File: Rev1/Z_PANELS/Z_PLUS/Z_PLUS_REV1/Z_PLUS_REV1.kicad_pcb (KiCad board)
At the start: 4 copper layers, 98 x 98 mm, 55 parts, among them IC1 LTC4316IDD#PBF, IC2 SM141K04TFV, IC3 SM141K04TFV, IC4 SM141K04TFV, IC5 SM141K04TFV, J1 F3311A7H121014E200, Q1 BSS138, Q2 BSS138, Q3 MBT2222ADW1T1, Q4 BSS138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

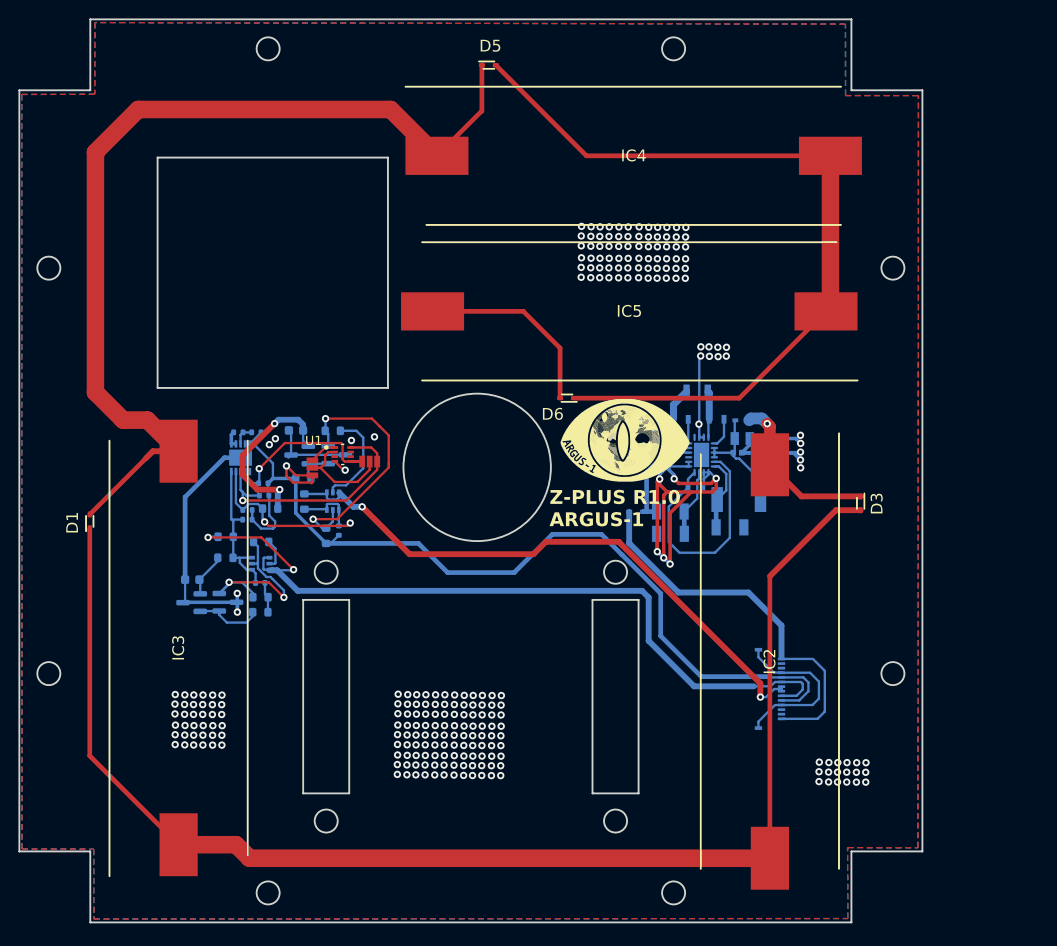
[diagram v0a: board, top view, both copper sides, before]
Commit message: finished Z minus board design
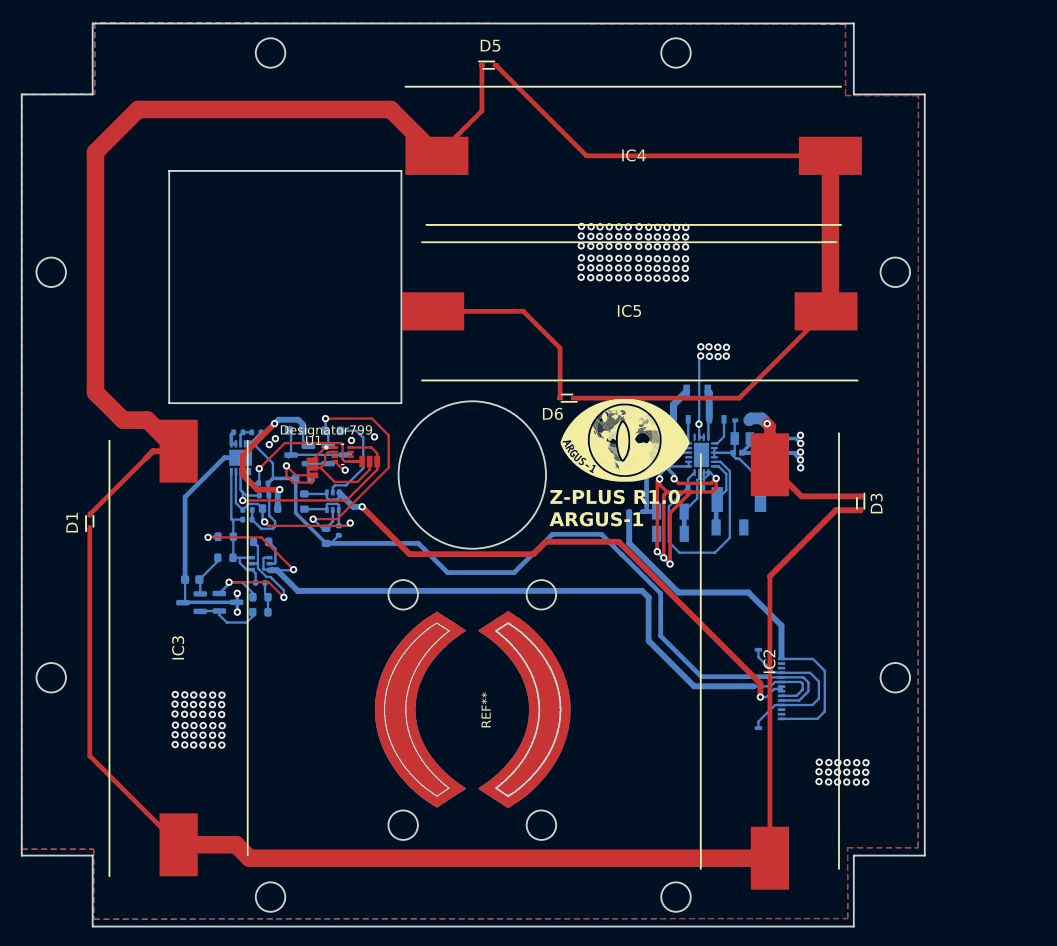
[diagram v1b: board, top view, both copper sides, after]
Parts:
- added REF**: Radio_antenna, Audio_Module:Radio_antenna, F.Cu at (171.7, 108.3)
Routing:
- net GND: vias 262 -> 154
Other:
- outline, holes or cut-outs redrawn

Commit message: fixed bug in Z minus
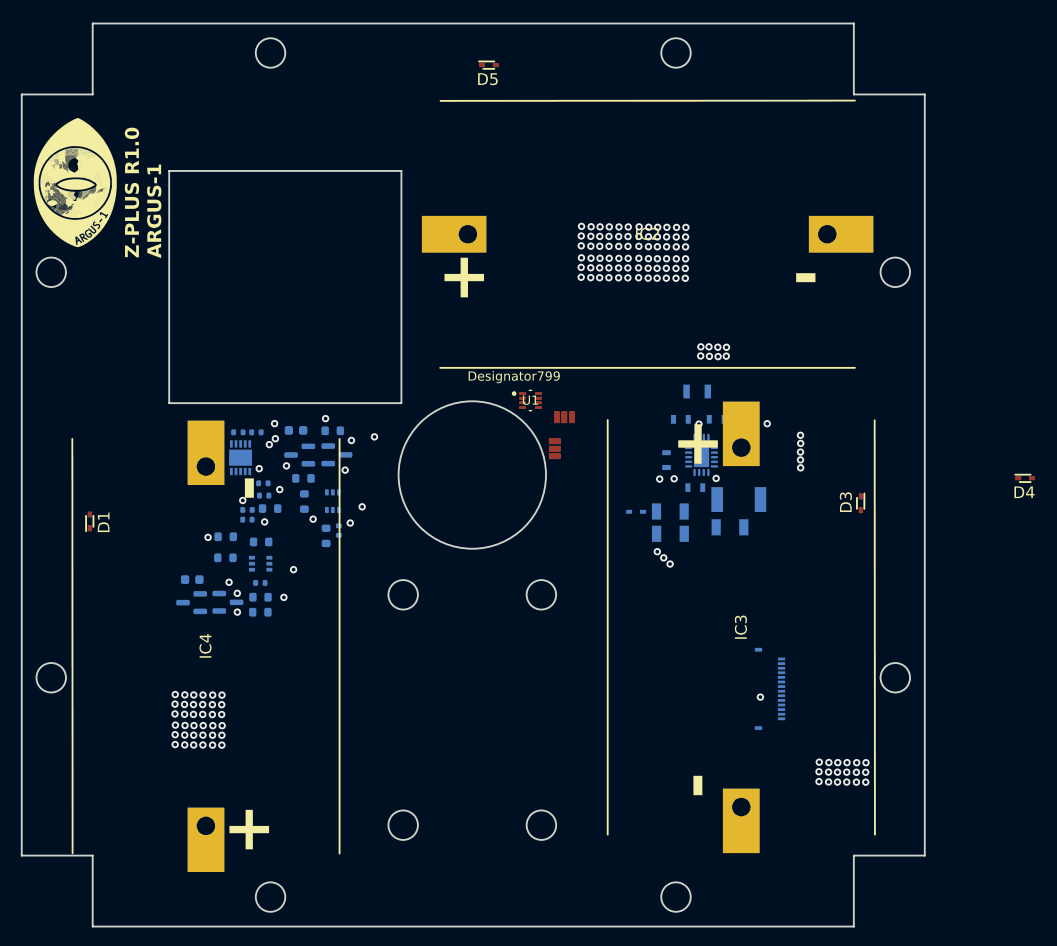
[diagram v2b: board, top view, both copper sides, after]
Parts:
- removed D6, D7: RB521S30T1G, AA_AUTO_LOADER:SODFL1608X70N
- removed IC5: SM141K04TFV, AA_AUTO_LOADER:SODFL490150X120N
- removed REF**: Radio_antenna, Audio_Module:Radio_antenna
- added D4: RB521S30T1G, AA_AUTO_LOADER:SODFL1608X70N, F.Cu at (229.7, 83.1)
- C3: value CL21A476MQYNNNE -> 47uF
- C4: value CL05A105KQ5NNNC -> 1uF
- C5, C8: value CL10A475KQ8NNNC -> 4.7uF
- IC2, IC3, IC4: value SM141K04TFV -> SM141K08TFV; footprint AA_AUTO_LOADER:SODFL490150X120N -> AA_AUTO_LOADER:SODFL520290X120N
- moved IC4 70.6 mm to (140.8, 101.3), turned to 90 degrees
- moved . 65.6 mm to (126.5, 51.2), turned to 90 degrees
- moved IC3 61.1 mm to (198.9, 99.3), turned to -90 degrees
- moved IC2 48.2 mm to (188.7, 56.6), turned to 0 degrees
- moved JP2 26.4 mm to (178.6, 79.9)
- moved JP1 21.7 mm to (179.7, 76.5)
- moved U1 21.2 mm to (176.0, 74.7)
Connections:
- C3 pad 1: GND -> Net-(U2-PVIN)
- C3 pad 2: Net-(U2-PVIN) -> GND
- C4 pad 1: GND -> Net-(U2-PVIN)
- C4 pad 2: Net-(U2-PVIN) -> GND
- C5 pad 1: GND -> Net-(U2-VCC)
- C5 pad 2: Net-(U2-VCC) -> GND
- C8 pad 1: GND -> Net-(U2-VOUT)
- C8 pad 2: Net-(U2-VOUT) -> GND
- D1 pad 1: Net-(IC2-NEG) -> /SOLAR_PANEL_ELECTRONICS/7023_vout
- D1 pad 2: Net-(IC3-NEG) -> Net-(IC2-NEG)
- D2 pad 1: VSOLAR -> Net-(IC2-NEG)
- D2 pad 2: Net-(U2-VOUT) -> Net-(IC3-NEG)
- D3 pad 1: /SOLAR_PANEL_ELECTRONICS/7023_vout -> Net-(U2-PVIN)
- D3 pad 2: Net-(IC2-NEG) -> /SOLAR_PANEL_ELECTRONICS/7023_vout
- D5 pad 1: Net-(IC3-NEG) -> VSOLAR
- D5 pad 2: Net-(IC4-NEG) -> Net-(U2-VOUT)
- IC4 pad 2: Net-(IC4-NEG) -> GND
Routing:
- net GND: track 169.3 -> 0.00 mm
- net Net-(IC2-NEG): track 146.5 -> 0.00 mm
- net Net-(IC3-NEG): track 103.1 -> 0.00 mm, vias 0 -> 1
- net +3.3V: track 102.1 -> 0.00 mm
- net Net-(IC4-NEG): track 88.1 -> 0.00 mm
- net SCL1_b4iso: track 86.0 -> 0.00 mm
- net SDA1_b4iso: track 65.2 -> 0.00 mm
- net VSOLAR: track 41.8 -> 0.00 mm
- net Net-(Q4-S): track 28.9 -> 0.00 mm, vias 2 -> 1
- net SDA_SUN: track 26.3 -> 0.00 mm
- net SDA_4001: track 26.3 -> 0.00 mm
- net Net-(U2-VCC): track 25.8 -> 0.00 mm
- net Net-(Q1-S): track 21.7 -> 0.00 mm
- net Net-(Q5-G): track 19.9 -> 0.00 mm
- net SCL_4001: track 19.4 -> 0.00 mm
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- removed copper zone on B.Cu, net GND
- removed copper zone on F.Cu, net GND

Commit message: fixed bugs and finished Z plus
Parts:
- added FL1: DXW21HN5011BL, AA_AUTO_LOADER:DXW21HN5011BL, B.Cu at (169.9, 95.7)
- added J2: 73412-0114, AA_AUTO_LOADER:73412-0110, B.Cu at (152.3, 93.2)
- added J3: Tape_Measure_Antenna, Audio_Module:Radio_antenna, F.Cu at (171.7, 108.3)
- C3: footprint AA_AUTO_LOADER:CAPC2012X135N -> Capacitor_SMD:C_0805_2012Metric
- C4: footprint AA_AUTO_LOADER:CAPC1005X55N -> Capacitor_SMD:C_0805_2012Metric
- C5, C8: footprint AA_AUTO_LOADER:CAPC1608X90N -> Capacitor_SMD:C_0805_2012Metric
- D2: moved to F.Cu
- D3, D5: moved to B.Cu
- R1, R10, R17, R2, R5, R6: footprint Resistor_SMD:R_0402_1005Metric -> Resistor_SMD:R_0805_2012Metric
- R11, R14, R15, R16, R18, R7, R8, R9: footprint Resistor_SMD:R_0603_1608Metric -> Resistor_SMD:R_0805_2012Metric
- R3, R4: footprint Resistor_SMD:R_0402_1005Metric -> Resistor_SMD:R_0805_2012Metric; moved to F.Cu
- moved D4 110.0 mm to (124.8, 116.5), turned to 90 degrees
- moved D1 83.2 mm to (196.7, 40.5), turned to 0 degrees
- moved . 78.3 mm to (142.4, 97.3), turned to -90 degrees
- moved R11 56.0 mm to (194.7, 113.1), turned to 180 degrees
- moved Q2 52.3 mm to (187.9, 115.7)
- moved R7 51.4 mm to (194.7, 116.1)
- moved C1 51.2 mm to (186.9, 113.1)
- moved R12 51.1 mm to (191.2, 106.2)
- moved R10 50.5 mm to (194.7, 110.3)
- moved R9 49.5 mm to (194.7, 108.3)
- moved C2 48.5 mm to (196.2, 94.2), turned to 0 degrees
- moved Q3 48.4 mm to (191.1, 111.6), turned to 0 degrees
- moved R8 47.9 mm to (191.1, 108.2), turned to 180 degrees
- moved R6 47.6 mm to (188.4, 67.6), turned to 90 degrees
- moved Q1 45.3 mm to (183.7, 116.7), turned to 180 degrees
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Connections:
- IC1 pad 7: SCL_4001 -> SDA_SUN
- IC1 pad 9: SDA_SUN -> SCL_4001
- JP2 pad 3: /SUN_SENSOR/+3.3v -> +3.3V
- Q1 pad 2: Net-(Q1-S) -> GND
- Q1 pad 3: GND -> Net-(Q1-D)
- Q2 pad 2: Net-(Q1-G) -> GND
- Q2 pad 3: GND -> Net-(Q1-G)
- Q3 pad 5: Net-(Q1-S) -> Net-(Q1-D)
- Q4 pad 2: Net-(Q4-S) -> GND
- Q4 pad 3: GND -> Net-(Q4-D)
- Q5 pad 2: Net-(Q4-G) -> GND
- Q5 pad 3: GND -> Net-(Q4-G)
- Q6 pad 5: Net-(Q4-S) -> Net-(Q4-D)
- R15 pad 2: Net-(Q4-S) -> Net-(Q4-D)
- R16 pad 2: Net-(Q4-S) -> Net-(Q4-D)
- R8 pad 1: Net-(Q1-S) -> Net-(Q1-D)
- R9 pad 2: Net-(Q1-S) -> Net-(Q1-D)
- U1 pad 1: /SUN_SENSOR/+3.3v -> +3.3V
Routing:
- net +3.3V: track 0.00 -> 149.7 mm, vias 0 -> 2
- net Net-(IC3-NEG): track 0.00 -> 110.8 mm, vias 1 -> 0
- net VSOLAR: track 0.00 -> 74.5 mm
- net Net-(IC2-NEG): track 0.00 -> 71.0 mm
- net SDA_SUN: track 0.00 -> 62.4 mm, vias 2 -> 0
- net SCL_SUN: track 0.00 -> 61.9 mm, vias 0 -> 2
- net /SOLAR_PANEL_ELECTRONICS/7023_vout: track 0.00 -> 41.7 mm, vias 1 -> 0
- net GND: track 0.00 -> 39.7 mm, vias 154 -> 502
- net SCL1_b4iso: track 0.00 -> 29.0 mm, vias 2 -> 0
- net Net-(U2-VOUT): track 0.00 -> 24.5 mm
- net Net-(Q4-D): track 0.00 -> 20.6 mm
- net Net-(Q1-D): track 0.00 -> 20.1 mm
- net SDA1_b4iso: track 0.00 -> 19.6 mm, vias 2 -> 0
- net SCL_4001: track 0.00 -> 19.5 mm, vias 1 -> 3
- net Net-(J2-SIGNAL): track 0.00 -> 19.0 mm
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- added copper zone on B.Cu, net GND
- added copper zone on F.Cu, net GND
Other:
- copper layers 4 -> 2
- rule pad_to_mask_clearance: 0 -> 0.0508

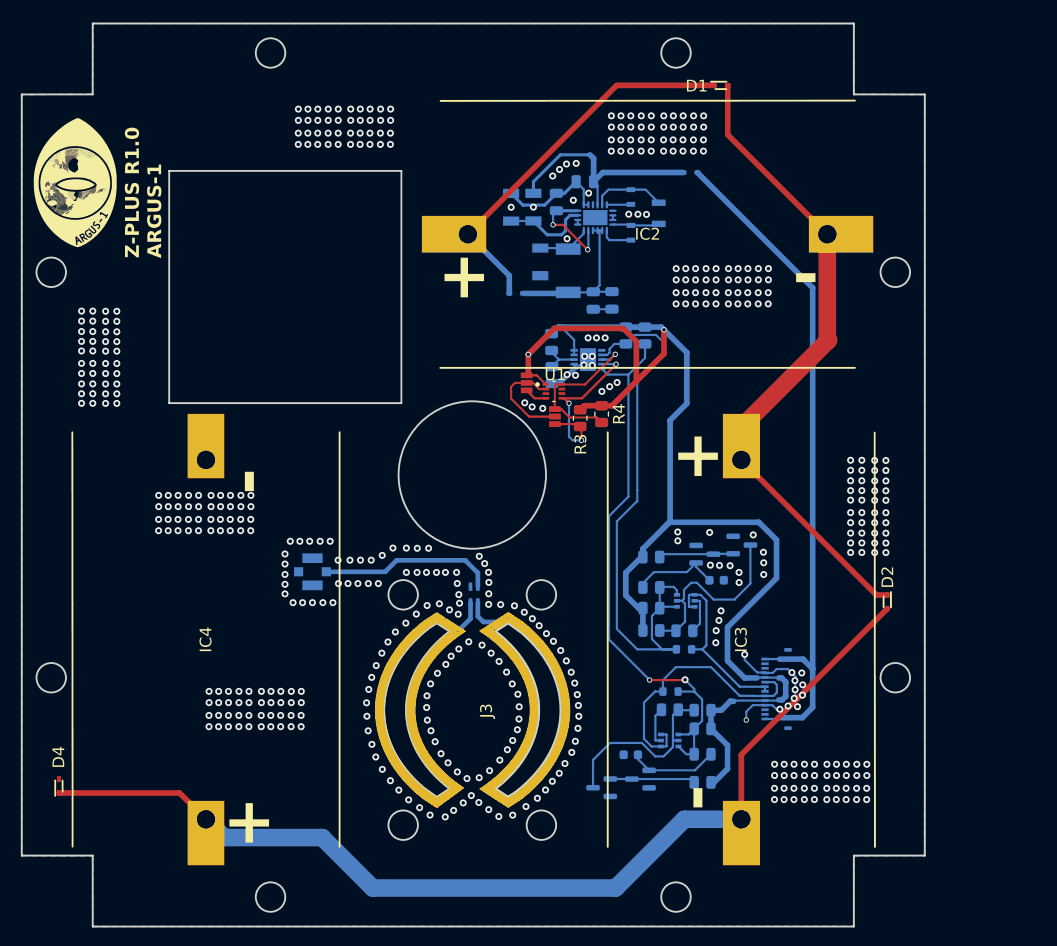
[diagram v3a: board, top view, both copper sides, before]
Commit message: CHANGED Resistor values for MPPC; added testpoints and silkscreen info
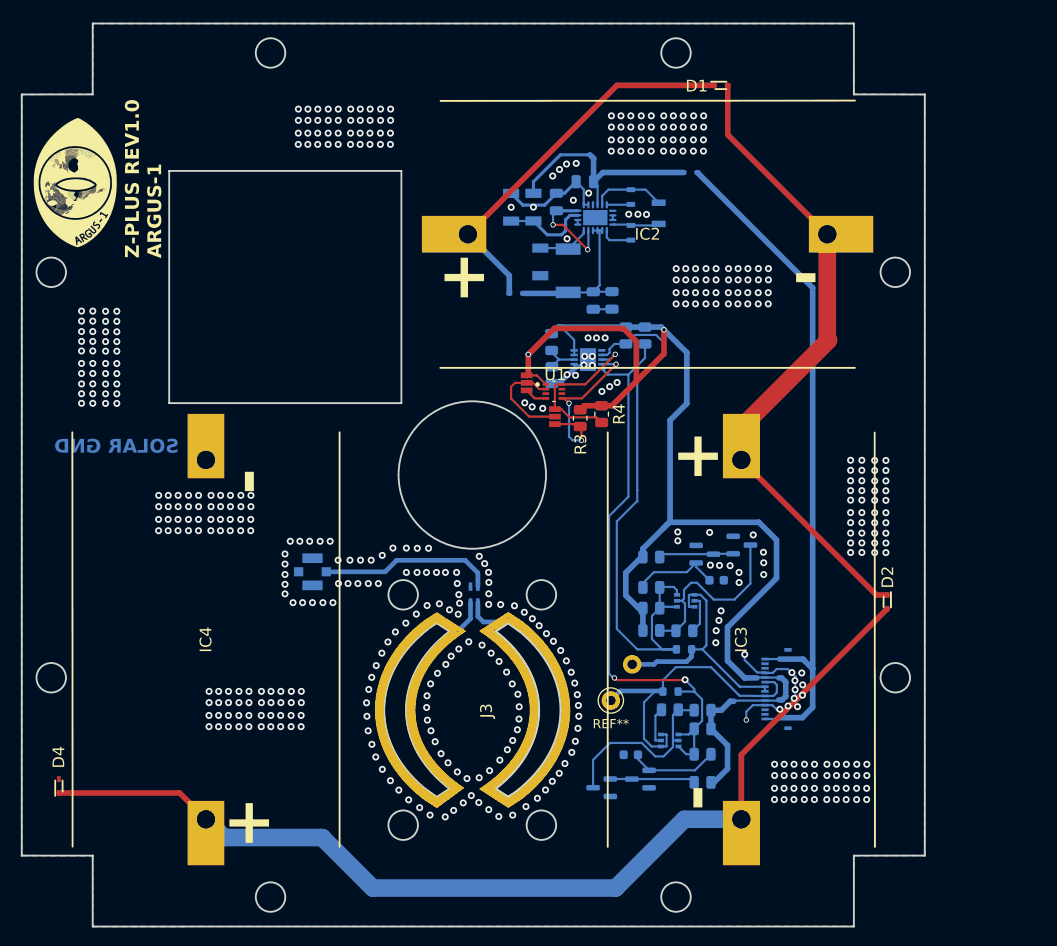
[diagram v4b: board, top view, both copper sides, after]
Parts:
- added ?: , , F.Cu at (187.0, 103.3)
- added REF**: Test_Point_D1.02mm, Source_Footprints:Test_Point_D1.02mm, F.Cu at (184.7, 107.2)
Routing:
- net SDA1_b4iso: track 19.6 -> 27.2 mm
- net SCL1_b4iso: track 29.0 -> 35.1 mm
- net SCL_SUN: track 61.9 -> 64.1 mm
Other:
- board text added: "R19=1.88*R20"
- board text added: "SOLAR GND"
- board text added: "SOLAR PWR (13.38V MPP)"
- board text added: "TP1 SDA_BISO"
- board text added: "TP2 SCL_BISO"
- board text added: "Z-PLUS REV1.0 ARGUS-1"
- board text removed: "Z-PLUS R1.0 ARGUS-1"

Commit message: made diode changes and schematic changes
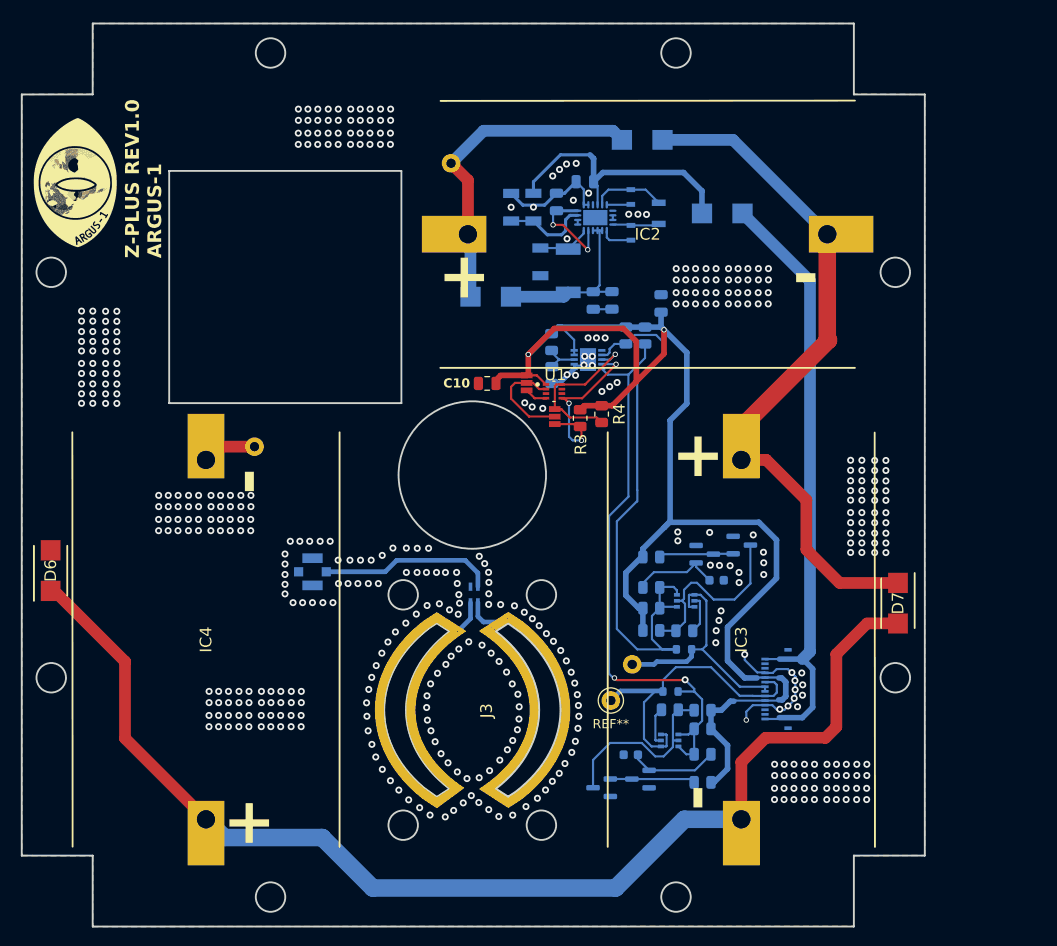
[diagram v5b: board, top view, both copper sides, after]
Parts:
- removed D1, D2, D3, D4, D5: RB521S30T1G, AA_AUTO_LOADER:SODFL1608X70N
- added ?: , , F.Cu at (167.4, 48.9)
- added ?: , , F.Cu at (146.0, 79.7)
- added C10: 0.1uF, Capacitor_SMD:C_0805_2012Metric, F.Cu at (171.3, 72.8)
- added C9: 0.1uF, Capacitor_SMD:C_0805_2012Metric, B.Cu at (190.2, 64.1)
- added D10: LSM115JE3_TR13, AA_AUTO_LOADER:DIOM5436X330N, B.Cu at (196.8, 54.4)
- added D6: LSM115JE3_TR13, AA_AUTO_LOADER:DIOM5436X330N, F.Cu at (123.9, 93.1)
- added D7: LSM115JE3_TR13, AA_AUTO_LOADER:DIOM5436X330N, F.Cu at (215.9, 96.7)
- added D8: LSM115JE3_TR13, AA_AUTO_LOADER:DIOM5436X330N, B.Cu at (188.1, 46.4)
- added D9: LSM115JE3_TR13, AA_AUTO_LOADER:DIOM5436X330N, B.Cu at (171.7, 63.4)
- R19: value CHV2010-FX-1005ELF -> 12M
- R20: value RC1206FR-072M49L -> 1M
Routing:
- net Net-(IC3-NEG): track 110.8 -> 130.4 mm
- net VSOLAR: track 74.5 -> 67.2 mm
- net +3.3V: track 149.7 -> 155.7 mm
- net /SOLAR_PANEL_ELECTRONICS/7023_vout: track 41.7 -> 35.8 mm
- net GND: track 39.7 -> 45.5 mm, vias 502 -> 462
- net Net-(IC2-NEG): track 71.0 -> 76.3 mm
- net Net-(U2-VOUT): track 24.5 -> 29.8 mm
- net Net-(U2-PVIN): track 17.6 -> 19.1 mm
